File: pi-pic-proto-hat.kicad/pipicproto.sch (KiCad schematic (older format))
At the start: 31 parts, among them J1 RUN/~PGM~, J10 Conn_01x13_Male, J2 Conn_SW1, J22 Conn_01x13_Male, J3 Conn_5P, J4 Conn_3V3P, J6 Barrel_Jack_Switch, J7 Conn_01x24_Male, J8 Conn_01x06_Male, J9 Conn_01x02_Male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

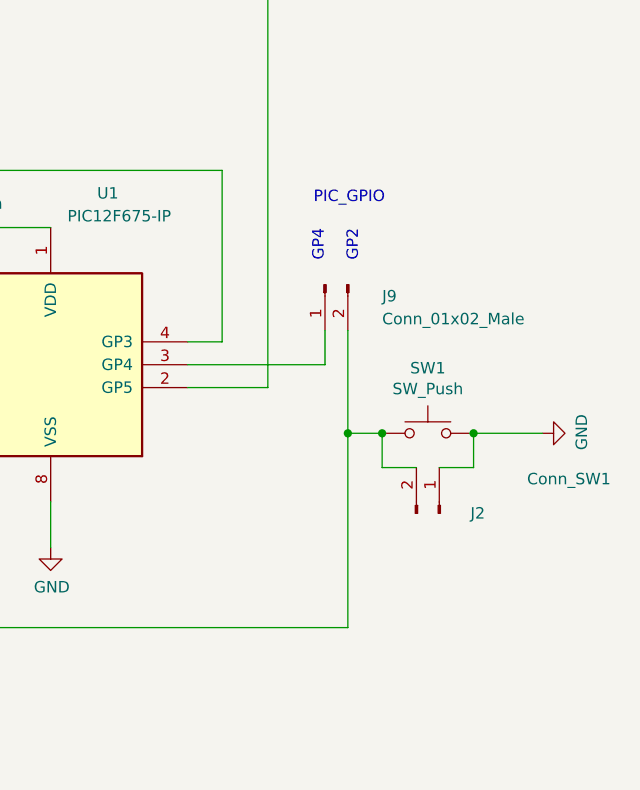
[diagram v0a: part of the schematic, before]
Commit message: V2.17: connect switch to GP4 instead of GP2
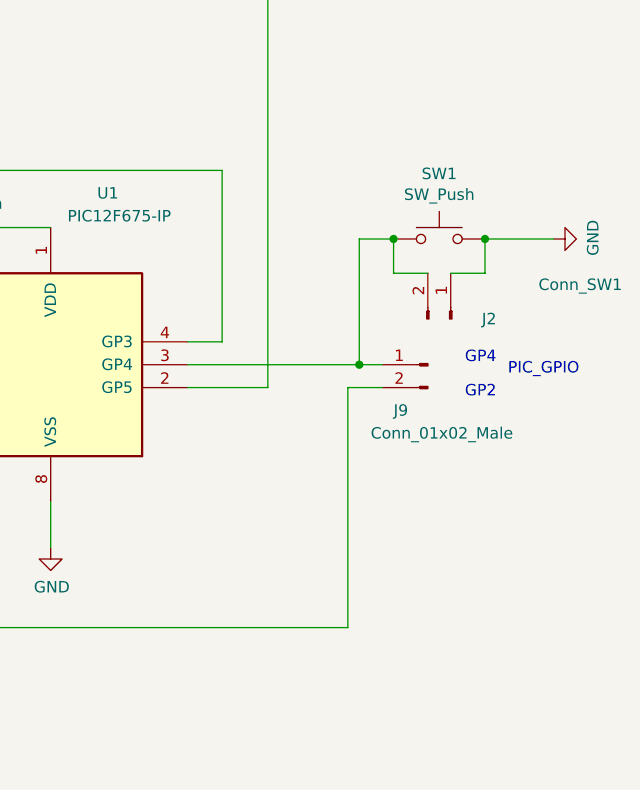
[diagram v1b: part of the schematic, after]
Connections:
- net at J9.1 (Pin_1), U1.3 (GP4): now also J2.2 (Pin_2), SW1.1
- net at J9.2 (Pin_2), U1.5 (GP2): no longer J2.2 (Pin_2), SW1.1
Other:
- moved on the sheet: J2, J9, SW1
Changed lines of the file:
@@
 Sheet 1 1
 Title "PI PIC Prototyping Area"
-Date "2020-07-24"
-Rev "2.16"
+Date "2020-07-25"
+Rev "2.17"
 Comp "Bernhard Bablok, Lothar Hiller"
 Comment1 "https://github.com/bablokb/pi-pic-proto-hat"
@@
 L Connector:Conn_01x02_Male J9
 U 1 1 5E2FB733
-P 9200 4250
-F 0 "J9" V 9250 4000 50  0000 R CNN
-F 1 "Conn_01x02_Male" V 9350 4000 50  0000 R CNN
-F 2 "Connector_PinHeader_2.54mm:PinHeader_1x02_P2.54mm_Vertical" H 9200 4250 50  0001 C CNN
-F 3 "~" H 9200 4250 50  0001 C CNN
-	1    9200 4250
-	0    -1   1    0
+P 9650 4600
+F 0 "J9" H 9800 4400 50  0000 R CNN
+F 1 "Conn_01x02_Male" H 9900 4300 50  0000 R CNN
+F 2 "Connector_PinHeader_2.54mm:PinHeader_1x02_P2.54mm_Vertical" H 9650 4600 50  0001 C CNN
+F 3 "~" H 9650 4600 50  0001 C CNN
+	1    9650 4600
+	-1   0    0    -1
 $EndComp
 $Comp
@@
 Wire Wire Line
 	5600 3750 5600 4200
-Wire Wire Line
-	8600 4600 9200 4600
-Text Notes 9150 3900 0    50   ~ 0
+Text Notes 10000 4650 0    50   ~ 0
 PIC_GPIO
 NoConn ~ 5600 4700
@@
 	6800 5650 6000 5650
 Wire Wire Line
-	9200 4600 9200 4450
-Wire Wire Line
 	7250 5750 9300 5750
-Wire Wire Line
-	9300 5750 9300 4900
-Text Notes 9200 4150 1    50   ~ 0
+Text Notes 9950 4600 2    50   ~ 0
 GP4
-Text Notes 9350 4150 1    50   ~ 0
+Text Notes 9950 4750 2    50   ~ 0
 GP2
 Wire Wire Line
@@
 L Switch:SW_Push SW1
 U 1 1 5F19E2FA
-P 9650 4900
-F 0 "SW1" H 9650 5185 50  0000 C CNN
-F 1 "SW_Push" H 9650 5094 50  0000 C CNN
-F 2 "user:SW_PUSH_SLIM_1x4" H 9650 5100 50  0001 C CNN
-F 3 "~" H 9650 5100 50  0001 C CNN
-	1    9650 4900
-	1    0    0    -1
-$EndComp
-Wire Wire Line
-	9450 4900 9300 4900
-Connection ~ 9300 4900
-Wire Wire Line
-	9300 4900 9300 4450
+P 9700 4050
+F 0 "SW1" H 9700 4335 50  0000 C CNN
+F 1 "SW_Push" H 9700 4244 50  0000 C CNN
+F 2 "user:SW_PUSH_SLIM_1x4" H 9700 4250 50  0001 C CNN
+F 3 "~" H 9700 4250 50  0001 C CNN
+	1    9700 4050
+	1    0    0    -1
+$EndComp
+Wire Wire Line
+	9500 4050 9350 4050
 $Comp
 L power:GND #PWR05
 U 1 1 5F1A4F9E
-P 10150 4900
-F 0 "#PWR05" H 10150 4650 50  0001 C CNN
-F 1 "GND" H 10155 4727 50  0000 C CNN
-F 2 "" H 10150 4900 50  0001 C CNN
-F 3 "" H 10150 4900 50  0001 C CNN
-	1    10150 4900
+P 10200 4050
+F 0 "#PWR05" H 10200 3800 50  0001 C CNN
+F 1 "GND" H 10205 3877 50  0000 C CNN
+F 2 "" H 10200 4050 50  0001 C CNN
+F 3 "" H 10200 4050 50  0001 C CNN
+	1    10200 4050
 	0    -1   -1   0
 $EndComp
 Wire Wire Line
-	9850 4900 10150 4900
+	9900 4050 10200 4050
 $Comp
 L Connector:Conn_01x02_Male J2
 U 1 1 5F1ABA22
-P 9700 5250
-F 0 "J2" V 9700 5450 50  0000 R CNN
-F 1 "Conn_SW1" V 9850 6000 50  0000 R CNN
-F 2 "Connector_PinHeader_2.54mm:PinHeader_1x02_P2.54mm_Vertical" H 9700 5250 50  0001 C CNN
-F 3 "~" H 9700 5250 50  0001 C CNN
-	1    9700 5250
+P 9750 4400
+F 0 "J2" V 9750 4600 50  0000 R CNN
+F 1 "Conn_SW1" V 9900 5150 50  0000 R CNN
+F 2 "Connector_PinHeader_2.54mm:PinHeader_1x02_P2.54mm_Vertical" H 9750 4400 50  0001 C CNN
+F 3 "~" H 9750 4400 50  0001 C CNN
+	1    9750 4400
 	0    1    -1   0
 $EndComp
 Wire Wire Line
-	9850 4900 9850 5050
-Wire Wire Line
-	9850 5050 9700 5050
-Connection ~ 9850 4900
-Wire Wire Line
-	9450 4900 9450 5050
-Wire Wire Line
-	9450 5050 9600 5050
-Connection ~ 9450 4900
+	9900 4050 9900 4200
+Wire Wire Line
+	9900 4200 9750 4200
+Connection ~ 9900 4050
+Wire Wire Line
+	9500 4050 9500 4200
+Wire Wire Line
+	9500 4200 9650 4200
+Connection ~ 9500 4050
 Wire Wire Line
 	1450 5950 1450 5850
@@
 	0    1    -1   0
 $EndComp
+Wire Wire Line
+	8600 4600 9350 4600
+Wire Wire Line
+	9300 5750 9300 4700
+Wire Wire Line
+	9300 4700 9450 4700
+Wire Wire Line
+	9350 4050 9350 4600
+Connection ~ 9350 4600
+Wire Wire Line
+	9350 4600 9450 4600
 $EndSCHEMATC

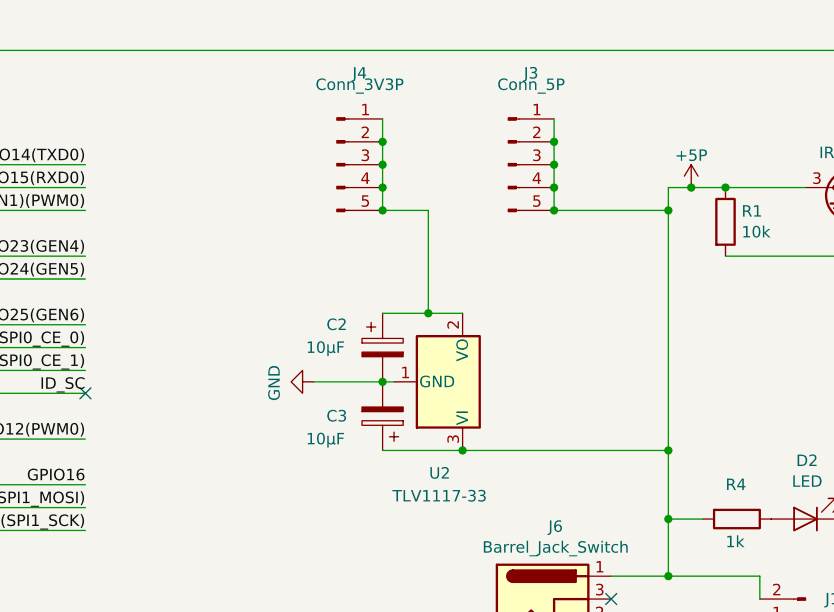
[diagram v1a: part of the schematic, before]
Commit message: V2.18: add 5VP and 3V3P connectors bottom left
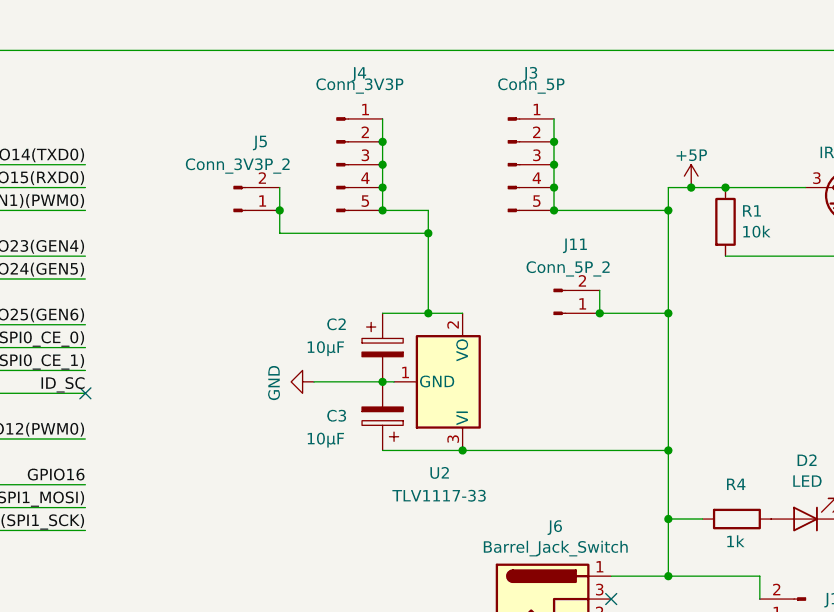
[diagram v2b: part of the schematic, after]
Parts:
- added J11: Conn_5P_2, Connector_PinHeader_2.54mm:PinHeader_1x02_P2.54mm_Vertical, symbol Connector:Conn_01x02_Male
- added J5: Conn_3V3P_2, Connector_PinHeader_2.54mm:PinHeader_1x02_P2.54mm_Vertical, symbol Connector:Conn_01x02_Male
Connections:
- net +5P: now also J11.1 (Pin_1), J11.2 (Pin_2)
- net at C2.1, J4.1 (Pin_1), J4.2 (Pin_2)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: now also J5.1 (Pin_1), J5.2 (Pin_2)
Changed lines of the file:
@@
 Title "PI PIC Prototyping Area"
 Date "2020-07-25"
-Rev "2.17"
+Rev "2.18"
 Comp "Bernhard Bablok, Lothar Hiller"
 Comment1 "https://github.com/bablokb/pi-pic-proto-hat"
@@
 Connection ~ 6500 1600
 Wire Wire Line
-	6500 1600 6500 2650
+	6500 1600 6500 2050
 Connection ~ 6500 2650
 Wire Wire Line
@@
 $EndComp
 Wire Wire Line
-	5450 2050 5450 1600
+	5450 2050 5450 1700
 Wire Wire Line
 	5450 1600 5250 1600
@@
 Wire Wire Line
 	9350 4600 9450 4600
+$Comp
+L Connector:Conn_01x02_Male J11
+U 1 1 5F207F86
+P 6000 2050
+F 0 "J11" H 6150 1750 50  0000 R CNN
+F 1 "Conn_5P_2" H 6250 1850 50  0000 R CNN
+F 2 "Connector_PinHeader_2.54mm:PinHeader_1x02_P2.54mm_Vertical" H 6000 2050 50  0001 C CNN
+F 3 "~" H 6000 2050 50  0001 C CNN
+	1    6000 2050
+	1    0    0    1
+$EndComp
+Wire Wire Line
+	6500 2050 6200 2050
+Wire Wire Line
+	6200 2050 6200 1950
+Connection ~ 6500 2050
+Wire Wire Line
+	6500 2050 6500 2650
+Connection ~ 6200 2050
+$Comp
+L Connector:Conn_01x02_Male J5
+U 1 1 5F219CE1
+P 4600 1600
+F 0 "J5" H 4750 1300 50  0000 R CNN
+F 1 "Conn_3V3P_2" H 4850 1400 50  0000 R CNN
+F 2 "Connector_PinHeader_2.54mm:PinHeader_1x02_P2.54mm_Vertical" H 4600 1600 50  0001 C CNN
+F 3 "~" H 4600 1600 50  0001 C CNN
+	1    4600 1600
+	1    0    0    1
+$EndComp
+Wire Wire Line
+	5450 1700 4800 1700
+Wire Wire Line
+	4800 1700 4800 1600
+Connection ~ 5450 1700
+Wire Wire Line
+	5450 1700 5450 1600
+Wire Wire Line
+	4800 1600 4800 1500
+Connection ~ 4800 1600
 $EndSCHEMATC

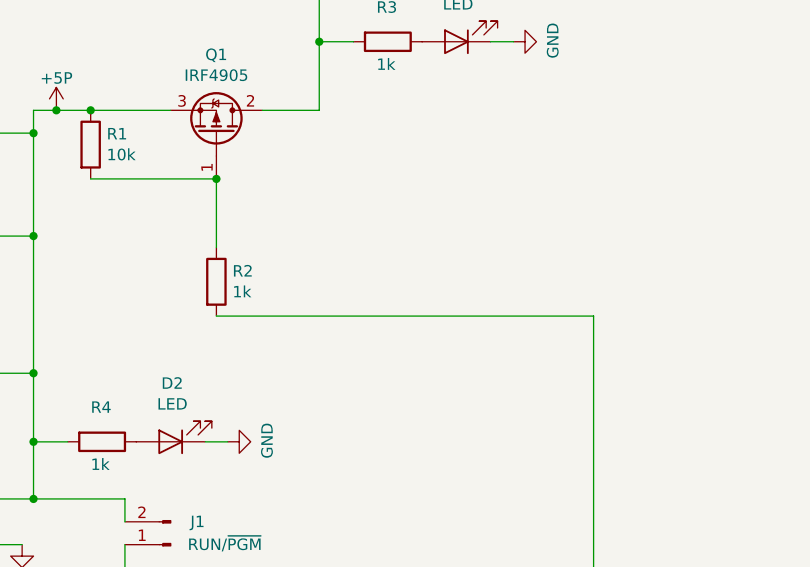
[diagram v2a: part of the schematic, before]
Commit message: V2.19: add GP5 connector
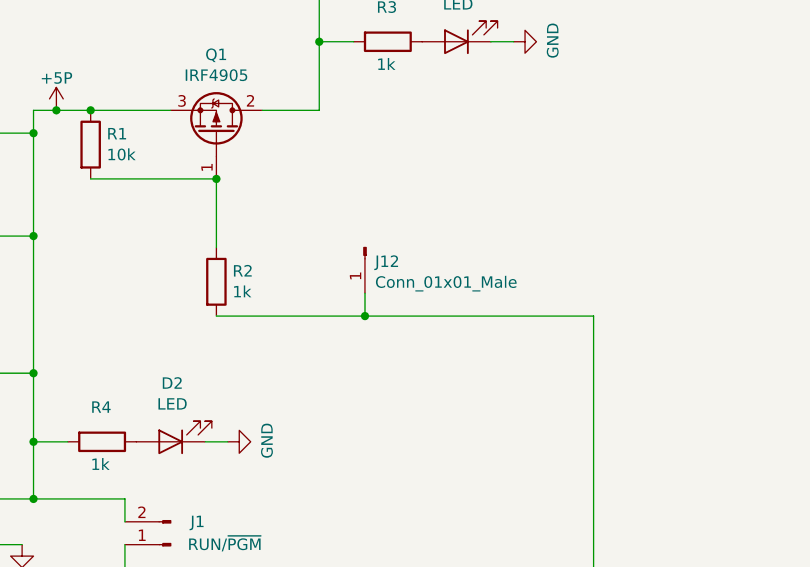
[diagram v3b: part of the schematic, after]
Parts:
- added J12: Conn_01x01_Male, Connector_PinHeader_2.54mm:PinHeader_1x01_P2.54mm_Vertical, symbol Connector:Conn_01x01_Male
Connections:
- net at R2.2, U1.2 (GP5): now also J12.1 (Pin_1)
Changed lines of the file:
@@
 Title "PI PIC Prototyping Area"
 Date "2020-07-25"
-Rev "2.18"
+Rev "2.19"
 Comp "Bernhard Bablok, Lothar Hiller"
 Comment1 "https://github.com/bablokb/pi-pic-proto-hat"
@@
 	8950 4700 8950 2400
 Wire Wire Line
-	8950 2400 7300 2400
+	8950 2400 7950 2400
 Text Label 5850 5300 2    50   ~ 0
 GPIO16
@@
 	4800 1600 4800 1500
 Connection ~ 4800 1600
+$Comp
+L Connector:Conn_01x01_Male J12
+U 1 1 5F23F4B8
+P 7950 2100
+F 0 "J12" V 8012 2144 50  0000 L CNN
+F 1 "Conn_01x01_Male" V 8103 2144 50  0000 L CNN
+F 2 "Connector_PinHeader_2.54mm:PinHeader_1x01_P2.54mm_Vertical" H 7950 2100 50  0001 C CNN
+F 3 "~" H 7950 2100 50  0001 C CNN
+	1    7950 2100
+	0    1    1    0
+$EndComp
+Wire Wire Line
+	7950 2400 7950 2300
+Connection ~ 7950 2400
+Wire Wire Line
+	7950 2400 7300 2400
 $EndSCHEMATC
